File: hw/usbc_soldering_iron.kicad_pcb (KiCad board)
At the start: 4 copper layers, 100 x 11 mm, 76 parts, among them J1 USB_C_Receptacle_USB2.0_14P, J10 TIP_G, J11 TIP_R, J12 TIP_B, J13 TIP_G, J14 TIP_R, J15 TIP_B, J16 TIP_G, J2 DBG, J3 LED RING, J4 OLED, J5 TIP_R, J6 TIP_B, J7 TIP_G, J8 TIP_R, J9 TIP_B, Q1 CSD16327Q3, U1 CH32X035F8U6, U10 AP63203WU, U11 SIQ-02FVS3, U2 TPA191Ax, U3 TPD4E05U06DQA, U5 SC7A20, U6 MT3608, U7 TLV333IDBVR, U8 IRS20752L, IRS20752L, NSG10752

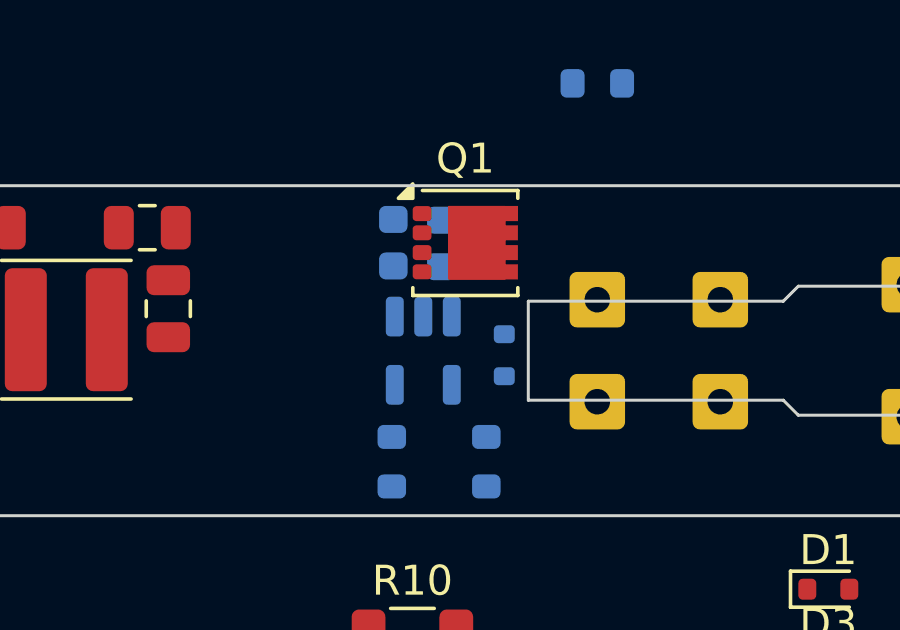
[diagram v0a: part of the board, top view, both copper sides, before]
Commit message: flyback diode to the tip
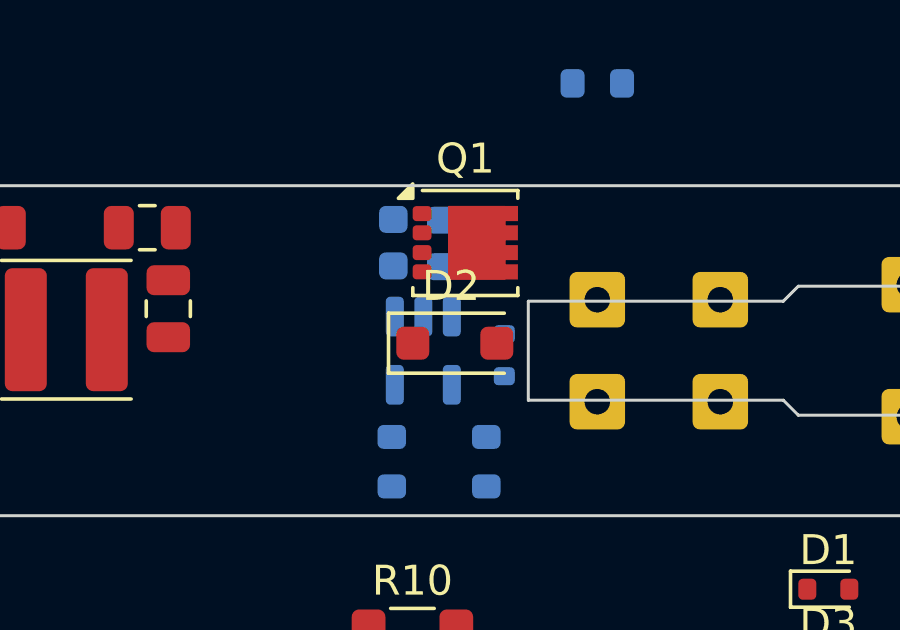
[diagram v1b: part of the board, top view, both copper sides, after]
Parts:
- added D2: SS24L, Diode_SMD:D_SOD-123F, F.Cu at (160.8, 152.4)
- J1: value USB_C_Receptacle_USB2.0_14P -> U263-163N-4OS1735

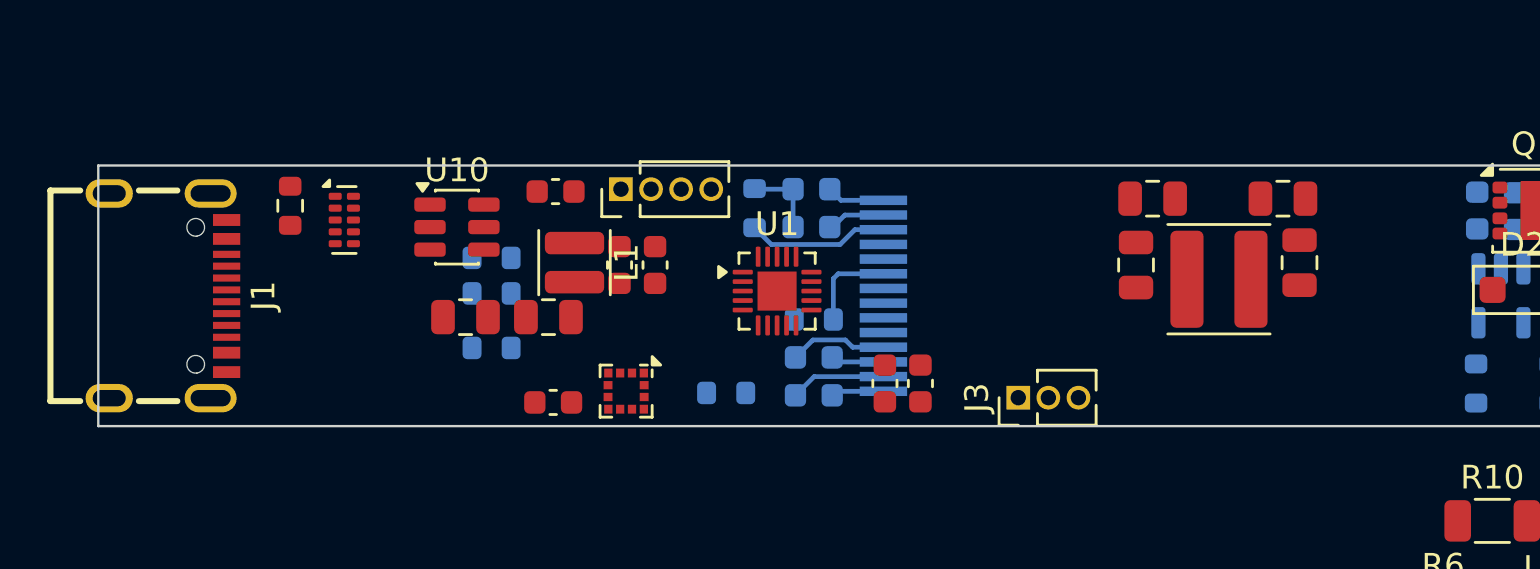
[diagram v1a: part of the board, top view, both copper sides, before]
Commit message: removed the diocane filter in favor of capacitors
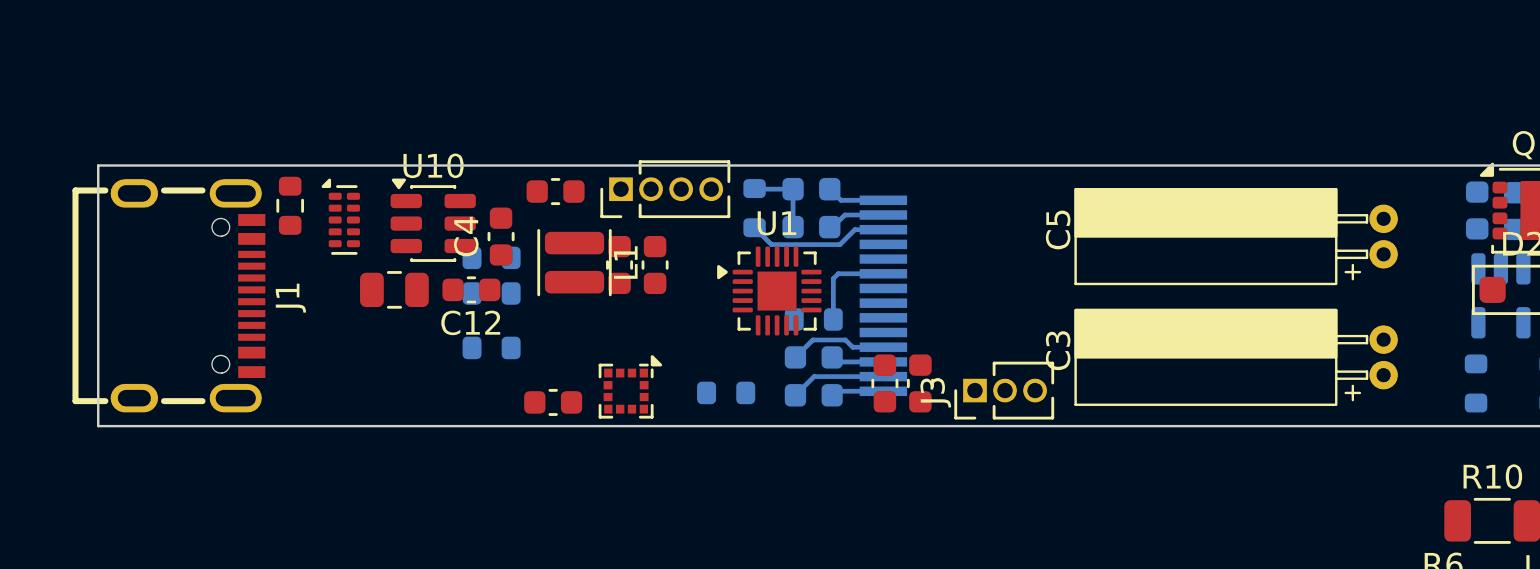
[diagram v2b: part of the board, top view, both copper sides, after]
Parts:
- removed C23, C25, C26, C28: 22u, Capacitor_SMD:C_0805_2012Metric
- removed L2: 2.2u, Inductor_SMD:L_Changjiang_FTC404030S
- added C3: 100u, Custom:CPol_Circular_Bent_D4mm_L11mm, F.Cu at (154.8, 155.3)
- added C4: 22u, Capacitor_SMD:C_0603_1608Metric, F.Cu at (117.5, 150.2)
- added C5: 100u, Custom:CPol_Circular_Bent_D4mm_L11mm, F.Cu at (154.8, 150.2)
- C12: footprint Capacitor_SMD:C_0805_2012Metric -> Capacitor_SMD:C_0603_1608Metric
- Q1: value CSD16327Q3 -> AGM403AP
- moved C12 3.45 mm to (116.2, 152.4)
- moved C6 3.21 mm to (113.0, 152.4)
- moved J3 1.85 mm to (137.5, 156.7)
- moved J1 1.06 mm to (104.5, 152.7)
- moved U10 1.01 mm to (114.6, 149.7)
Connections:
- R10 pad 2: Net-(U2-IN-) -> Net-(Q1-D)
- U2 pad 5: Net-(U2-IN-) -> Net-(Q1-D)

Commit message: different smaller capacitor
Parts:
- added C11: 47u, Custom:CPol_Circular_Bent_D5mm_L6mm, F.Cu at (148.4, 155.3)
- added C14: 47u, Custom:CPol_Circular_Bent_D5mm_L6mm, F.Cu at (148.4, 150.1)
- C3, C5: value 100u -> 47u; footprint Custom:CPol_Circular_Bent_D4mm_L11mm -> Custom:CPol_Circular_Bent_D5mm_L6mm
- moved C5 4.91 mm to (149.8, 150.1), turned to -90 degrees
- moved C3 4.91 mm to (149.8, 155.3), turned to -90 degrees
- moved J3 0.45 mm to (137.9, 156.9), turned to 180 degrees

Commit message: different capacitors and new bom
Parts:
- removed C11, C14: 47u, Custom:CPol_Circular_Bent_D5mm_L6mm
- C3: value 47u -> 100u; footprint Custom:CPol_Circular_Bent_D5mm_L6mm -> Custom:CPol_Circular_Bent_D6.3mm_L8mm_L
- C5: value 47u -> 100u; footprint Custom:CPol_Circular_Bent_D5mm_L6mm -> Custom:CPol_Circular_Bent_D6.3mm_L8mm_R
- moved C3 5.32 mm to (147.0, 150.8)
- moved C5 4.79 mm to (145.1, 150.8)
- moved J3 2.00 mm to (139.9, 156.8), turned to -90 degrees

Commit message: new filter design, may work lmao
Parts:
- removed R25: 1k, Resistor_SMD:R_0603_1608Metric
- added C11: 10u, Capacitor_SMD:C_1210_3225Metric, F.Cu at (152.4, 150.7)
- added C14: 10u, Capacitor_SMD:C_1210_3225Metric, F.Cu at (155.7, 155.5)
- added C21: 10u, Capacitor_SMD:C_1210_3225Metric, F.Cu at (155.7, 150.7)
- added C23: 10u, Capacitor_SMD:C_1210_3225Metric, F.Cu at (152.4, 155.5)
- added L2: 2.2u, Inductor_SMD:L_Changjiang_FNR4030S, F.Cu at (148.4, 154.0)
- C3: footprint Custom:CPol_Circular_Bent_D6.3mm_L8mm_L -> Custom:CP-SMD_L7.3-W4.3-FD
- C5: value 100u -> 10u; footprint Custom:CPol_Circular_Bent_D6.3mm_L8mm_R -> Capacitor_SMD:C_1210_3225Metric
- moved D2 4.26 mm to (161.7, 156.6)
- moved C3 4.16 mm to (143.6, 153.2)
- moved C5 3.40 mm to (148.4, 150.0), turned to 0 degrees
- moved Q1 0.37 mm to (160.7, 149.2)
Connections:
- C27 pad 2: Net-(C27-Pad2) -> /TC_FB
- C3 pad 1: Net-(Q1-D) -> Net-(U2-IN-)
- C5 pad 1: Net-(Q1-D) -> Net-(U2-IN-)
- Q1 pad 5: Net-(Q1-D) -> /VDRV
- R10 pad 2: Net-(Q1-D) -> Net-(U2-IN-)
- R24 pad 2: Net-(C27-Pad2) -> /TC_FB
- U2 pad 5: Net-(Q1-D) -> Net-(U2-IN-)
- U7 pad 1: Net-(C27-Pad2) -> /TC_FB
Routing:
- net GND: vias 0 -> 9

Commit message: some component changes
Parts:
- removed the D4 at (173.2, 165.6)
- removed the J3 at (139.9, 156.8)
- removed the R6 at (157.3, 165.5)
- removed the R8 at (157.3, 168.0)
- removed the U2 at (161.6, 166.1)
- added U7: INA226, Package_SO:VSSOP-10_3x3mm_P0.5mm, F.Cu at (137.8, 154.1)
- R11: renamed from R10; value 1.5m -> 2m
- moved C12 27.7 mm to (140.3, 153.6), turned to -90 degrees
- moved R11 24.2 mm to (138.7, 149.6)
- renumbered C27 to C10, C12 to C11, C7 to C12, C3 to C13, C15 to C14, C5 to C15, C11 to C19, C19 to C20, C14 to C21, C20 to C22, C21 to C23, C23 to C24, C8 to C25, C29 to C26, C13 to C3, C22 to C4, C6 to C5, C9 to C6, C10 to C7, C24 to C8, C4 to C9, D6 to D1, D5 to D2, D1 to D3, D3 to D4, D2 to D5, J11 to J10, J12 to J11, J13 to J12, J14 to J13, J15 to J14, J16 to J15, J4 to J3, J5 to J4, J6 to J5, J7 to J6, J8 to J7, J9 to J8, J10 to J9, R24 to R10, R19 to R14, R21 to R15, R11 to R6, R15 to R8, R20 to R9, U5 to U1, U1 to U2, U11 to U4, U10 to U5, U7 to U6, U6 to U8, U8 to U9
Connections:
- U1 pad 10: unconnected-(U5-~{CS}-Pad10) -> +3.3V
- U1 pad 11: +3.3V -> unconnected-(U1-NC-Pad11)
- U2 pad 10: /LED_RING -> unconnected-(U2-PB0-Pad10)
- U2 pad 15: unconnected-(U1-PB12-Pad15) -> /POW_ALERT
- U2 pad 4: /CURR_FB -> unconnected-(U2-PA2-Pad4)

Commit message: boxed version
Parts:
- removed J10, J13, J7: TIP_R, Connector_Wire:SolderWire-0.25sqmm_1x01_D0.65mm_OD1.7mm
- removed J11, J14, J8: TIP_B, Connector_Wire:SolderWire-0.25sqmm_1x01_D0.65mm_OD1.7mm
- removed J12, J15, J6, J9: TIP_G, Connector_Wire:SolderWire-0.25sqmm_1x01_D0.65mm_OD1.7mm
- added H1: MountingHole, MountingHole:MountingHole_2.2mm_M2_DIN965, F.Cu at (103.5, 131.2)
- added H2: MountingHole, MountingHole:MountingHole_2.2mm_M2_DIN965, F.Cu at (167.5, 131.2)
- added H3: MountingHole, MountingHole:MountingHole_2.2mm_M2_DIN965, F.Cu at (167.5, 155.2)
- added H4: MountingHole, MountingHole:MountingHole_2.2mm_M2_DIN965, F.Cu at (103.5, 155.2)
- added J16: TIP_CONN, TerminalBlock_Phoenix:TerminalBlock_Phoenix_MKDS-1,5-3_1x03_P5.00mm_Horizontal, F.Cu at (164.8, 148.6)
- C10, C6, C8, D2, R10, R2, R3, R7, R8, R9, U4, U6: moved to F.Cu
- C20, C22: moved to B.Cu
- J2: footprint Connector_PinHeader_1.27mm:PinHeader_1x04_P1.27mm_Vertical -> Connector_PinHeader_2.54mm:PinHeader_1x04_P2.54mm_Vertical
- J4: value TIP_R -> GPIO; footprint Connector_Wire:SolderWire-0.25sqmm_1x01_D0.65mm_OD1.7mm -> Connector_PinHeader_2.54mm:PinHeader_1x04_P2.54mm_Vertical
- J5: value TIP_B -> DISP; footprint Connector_Wire:SolderWire-0.25sqmm_1x01_D0.65mm_OD1.7mm -> Connector_PinSocket_2.54mm:PinSocket_1x04_P2.54mm_Vertical
- moved J5 62.0 mm to (114.9, 139.3), turned to 0 degrees
- moved D1 61.4 mm to (122.2, 132.8)
- moved J4 61.2 mm to (109.3, 130.2)
- moved R15 39.5 mm to (148.1, 137.5), turned to 180 degrees
- moved R7 38.0 mm to (127.0, 144.7), turned to 180 degrees
- moved U8 37.4 mm to (147.6, 134.9)
- moved C6 37.2 mm to (124.0, 144.7), turned to 180 degrees
- moved D4 35.6 mm to (155.2, 132.4), turned to 180 degrees
- moved D3 35.2 mm to (150.5, 133.8), turned to 90 degrees
- moved U9 34.1 mm to (155.3, 134.9)
- moved L3 33.6 mm to (147.6, 132.4), turned to 180 degrees
- moved R14 30.9 mm to (150.5, 136.7), turned to -90 degrees
- moved C26 29.4 mm to (161.2, 133.7)
- moved C25 29.2 mm to (152.3, 134.9), turned to -90 degrees
- moved C3 26.5 mm to (132.9, 134.2)
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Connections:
- J4 pad 1: /RED -> /PA2
- J5 pad 1: /BLUE -> /SDA
- U2 pad 10: unconnected-(U2-PB0-Pad10) -> /PB0
- U2 pad 4: unconnected-(U2-PA2-Pad4) -> /PA2
- U2 pad 5: unconnected-(U2-PA3-Pad5) -> /PA3
- U2 pad 6: unconnected-(U2-PA4-Pad6) -> /PA4
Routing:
- net Net-(J3-Pin_12): track 5.99 -> 0.00 mm
- net Net-(J3-Pin_4): track 4.14 -> 0.00 mm
- net Net-(J3-Pin_2): track 4.04 -> 0.00 mm
- net Net-(J3-Pin_9): track 3.92 -> 0.00 mm
- net GND: track 3.24 -> 0.00 mm, vias 9 -> 0
- net Net-(J3-Pin_13): track 2.47 -> 0.00 mm
- net Net-(J3-Pin_14): track 2.46 -> 0.00 mm
- net Net-(J3-Pin_3): track 2.24 -> 0.00 mm
- net Net-(J3-Pin_1): track 2.23 -> 0.00 mm
- removed copper zone on In2.Cu, net GND
- removed copper zone on In1.Cu, net VBUS
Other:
- board size 100 x 11 mm -> 70 x 30 mm

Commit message: test pads
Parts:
- added TP1: VBUS, TestPoint:TestPoint_Pad_D1.5mm, F.Cu at (101.1, 119.1)
- added TP2: GND, TestPoint:TestPoint_Pad_D1.5mm, F.Cu at (101.2, 124.1)
- added TP3: TIP, TestPoint:TestPoint_Pad_D1.5mm, F.Cu at (104.7, 120.5)
- added TP4: DRIVE, TestPoint:TestPoint_Pad_D1.5mm, F.Cu at (145.9, 137.8)
- added TP5: GATE, TestPoint:TestPoint_Pad_D1.5mm, F.Cu at (108.3, 120.5)
- added TP6: TC, TestPoint:TestPoint_Pad_D1.5mm, F.Cu at (108.3, 124.1)
- added TP7: NTC, TestPoint:TestPoint_Pad_D1.5mm, F.Cu at (111.8, 120.5)
- added TP8: 3V3, TestPoint:TestPoint_Pad_D1.5mm, F.Cu at (115.9, 152.2)
- moved C10 9.52 mm to (152.8, 155.4), turned to -90 degrees
- moved R14 6.54 mm to (144.8, 133.5), turned to 90 degrees
- moved L3 6.20 mm to (142.4, 135.8), turned to 0 degrees
- moved U8 5.89 mm to (141.9, 133.4), turned to 180 degrees
- moved D3 5.64 mm to (145.2, 135.8), turned to 180 degrees
- moved D2 5.44 mm to (163.0, 156.0), turned to -90 degrees
- moved C25 4.50 mm to (147.8, 135.1), turned to 90 degrees
- moved R15 4.39 mm to (146.3, 133.5), turned to -90 degrees
- moved C7 3.20 mm to (109.2, 150.3), turned to 180 degrees
- moved L1 2.60 mm to (112.8, 152.2), turned to 0 degrees
- moved U5 2.32 mm to (109.2, 152.8)
- moved C11 2.02 mm to (112.9, 156.1)
- moved C9 1.56 mm to (112.9, 154.6), turned to 180 degrees
- moved R9 1.28 mm to (155.8, 155.4), turned to -90 degrees
- moved R10 1.14 mm to (154.3, 155.4), turned to -90 degrees
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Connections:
- net /VDRV renamed /VTIP
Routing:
- net +3.3V: track 0.00 -> 10.6 mm, vias 0 -> 5
- net /TC_FB: track 0.00 -> 9.57 mm
- net Net-(U6--): track 0.00 -> 4.83 mm
- net /VDRIVE: track 0.00 -> 4.16 mm
- net Net-(D2-K): track 0.00 -> 3.97 mm
- net Net-(U5-SW): track 0.00 -> 3.61 mm
- net Net-(U8-FB): track 0.00 -> 3.36 mm
- net Net-(U5-BST): track 0.00 -> 2.59 mm
- net VBUS: vias 0 -> 2
- net GND: vias 0 -> 9
- added copper zone on F.Cu, net +3.3V
- added copper zone on F.Cu, net GND
- added copper zone on F.Cu, net Net-(D3-A)
- added copper zone on F.Cu, net Net-(U5-SW)
- added copper zone on F.Cu, net VBUS
